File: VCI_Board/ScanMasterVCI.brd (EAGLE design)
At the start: 53 x 39.4 mm, 81 parts, among them IC1 XMEGA16A4A, Q1 MMBT4403, Q10 ZXMP6A17G, Q2 MMBT3904, Q3 MMBT3904, Q4 MMBT3904, Q5 MMBT3904, Q6 MMBT3904, Q7 NTZD5110N, Q8 NTZD5110N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

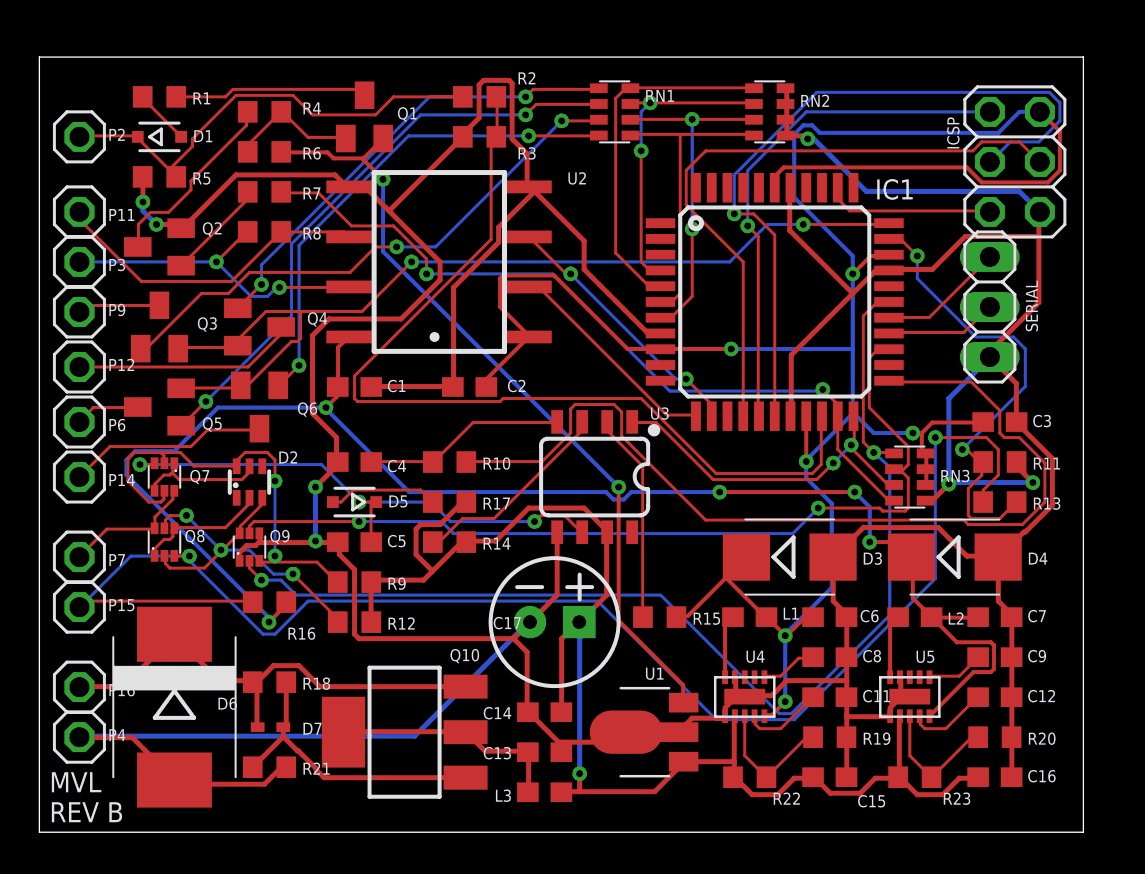
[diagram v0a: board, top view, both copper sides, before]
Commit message: Added Mini USB connector, beefed up traces
Doing more corrections that needed doing, +12V/GND traces are all 12 mil now, +5V/+8V/+3.3V traces are all 10 mil. Kept the rest as 6 mil for now. Rather than use a separate IC to do proper RS-232 communication to a PC, I am instead just going to use a Mini USB connector for PC connection based on what I've seen in the XMEGA data sheet. Changed the ICSP header to be a PDI header, since XMEGA apparently can't be programmed over ICSP.
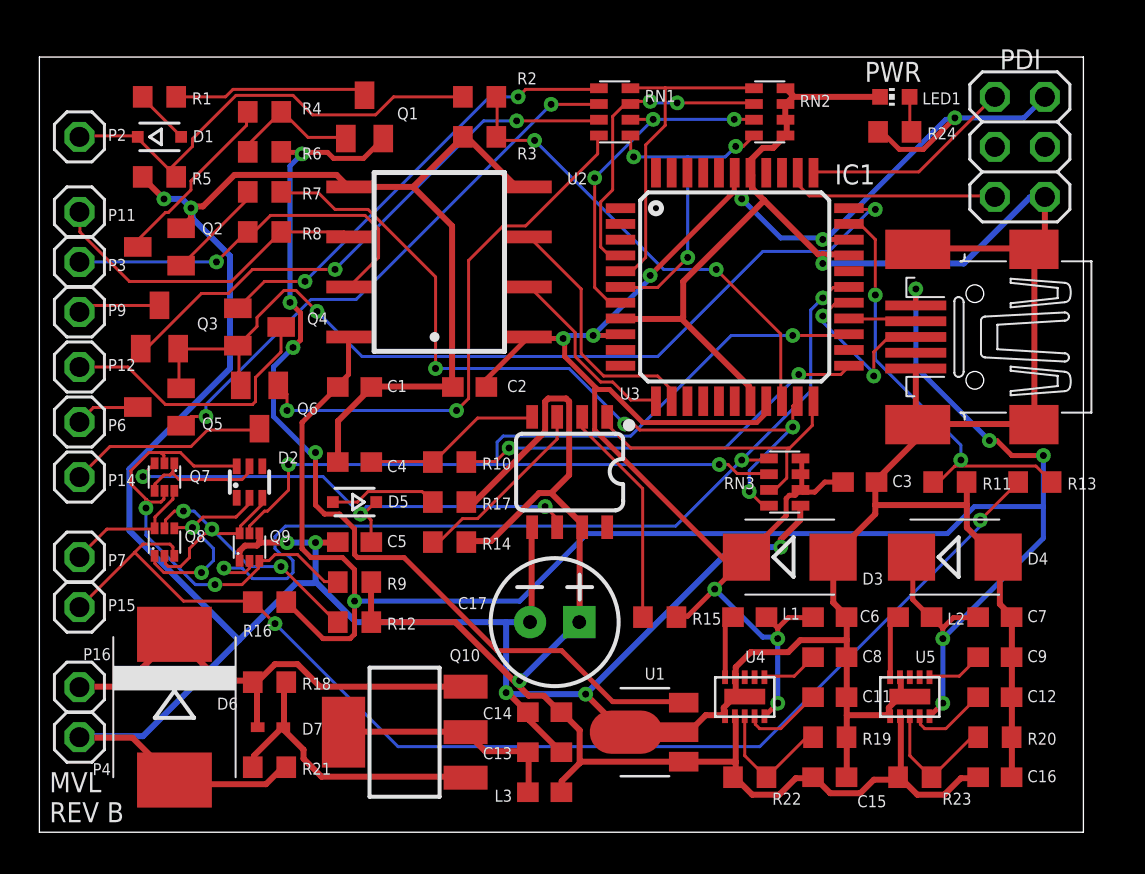
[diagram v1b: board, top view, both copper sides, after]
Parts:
- removed ICSP: (no value), pinhead:2X03
- removed SERIAL: (no value), pinhead:1X03
- added LED1: (no value), led:CHIP-LED0603
- added PDI: (no value), pinhead:2X03
- added R24: 120, resistor:R0603
- added X1: MINI-USB-SCHIELD-32005-201, con-cypressindustries:32005-201
- C13: value 0.1uF -> 0.1uF 25V
- C14: value 330pF -> 330pF 16V
- C17: value 100uF -> 100uF 25V
- D3: value SMLVT3V3 -> SMBJ3V3HE3
- moved C3 7.74 mm to (41.7, 17.8)
- moved RN3 6.36 mm to (37.8, 17.8)
- moved R11 2.74 mm to (46.2, 17.8)
- moved IC1 2.17 mm to (35.3, 27.7)
- moved R13 2.05 mm to (50.5, 17.8)
- moved U3 1.30 mm to (26.9, 18.3)
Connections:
- removed net MISO: IC1.16, ICSP.1
- removed net MOSI: IC1.15, ICSP.4
- removed net PC-RX: IC1.26, SERIAL.2
- removed net PC-TX: IC1.27, SERIAL.1
- removed net RESET: IC1.35, ICSP.5
- removed net SCK: IC1.17, ICSP.3
- new net N$2: LED1.A, R24.1
- new net N$24: IC1.27, X1.3
- new net N$25: IC1.26, X1.4
- new net PDI_CLK: IC1.35, PDI.5
- new net PDI_DATA: IC1.34, PDI.1
- net +3V3: now also PDI.2, R24.2; no longer ICSP.2
- net +5V: now also X1.5
- net GND: now also LED1.C, PDI.6, X1.1, X1.M1, X1.M2, X1.M3, X1.M4; no longer ICSP.6, SERIAL.3
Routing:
- net SCK: track 37.5 -> 0.00 mm, vias 1 -> 0
- net MOSI: track 32.7 -> 0.00 mm
- net MISO: track 26.2 -> 0.00 mm, vias 1 -> 0
- net ISO-K-TX: track 47.3 -> 21.5 mm, vias 0 -> 2
- net +3V3: track 119.8 -> 97.4 mm, vias 6 -> 9
- net J1850VPW-RX: track 46.4 -> 24.1 mm, vias 0 -> 2
- net +5V: track 77.4 -> 95.1 mm, vias 5 -> 6
- net J1962-15: track 75.8 -> 61.3 mm
- net PDI_CLK: track 0.00 -> 10.9 mm
- net PDI_DATA: track 0.00 -> 10.8 mm
- net SCI-A-TX-EN: track 56.4 -> 46.3 mm, vias 2 -> 3
- net N$24: track 0.00 -> 9.41 mm, vias 0 -> 2
- net +8V: track 40.1 -> 49.4 mm, vias 2 -> 4
- net RESET: track 8.57 -> 0.00 mm
- net +12V: track 70.8 -> 77.9 mm
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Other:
- board text added: "PWR"

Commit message: Added extra protection and pull-down resistors to USB circuit, added a pull-up resistor to PDI circuit.
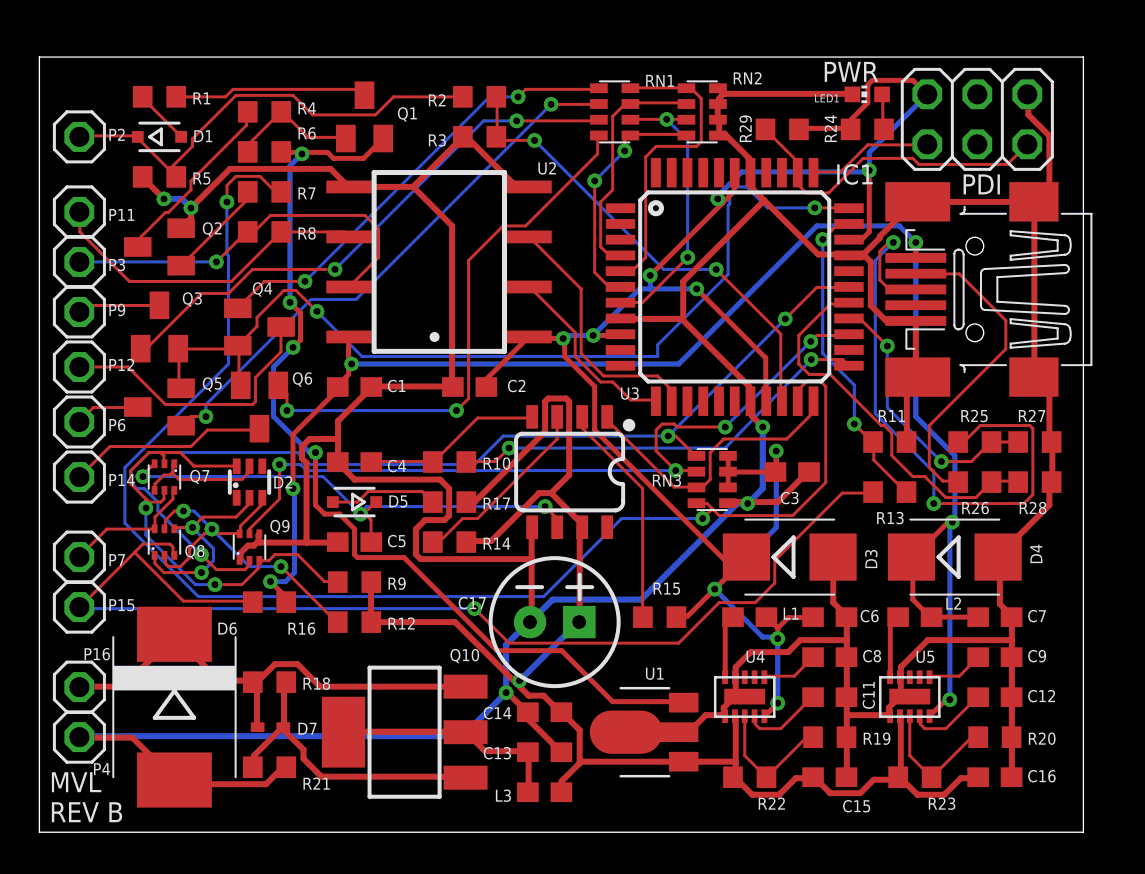
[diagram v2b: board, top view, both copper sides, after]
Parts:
- added R25, R26: 33, adafruit:R0603
- added R27, R28: 15k, adafruit:R0603
- added R29: 1k, adafruit:R0603
- IC1: value XMEGA16A4A -> XMEGA16A4U
- LED1: value (none) -> RED
- moved R13 7.38 mm to (43.2, 17.3)
- moved RN3 3.69 mm to (34.2, 17.9)
- moved R11 3.66 mm to (43.2, 19.8)
- moved C3 3.47 mm to (38.2, 18.3)
- moved RN2 3.43 mm to (33.7, 36.6)
- moved PDI 2.57 mm to (47.6, 36.2), turned to 0 degrees
- moved X1 2.41 mm to (47.5, 27.6)
- moved LED1 1.40 mm to (42.0, 37.5)
- moved R24 1.40 mm to (42.0, 35.7)
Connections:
- new net USB_D+: IC1.26, R25.2, R27.1
- new net USB_D-: IC1.27, R26.2, R28.1
- net +3V3: now also R29.2
- net GND: now also R27.2, R28.2
- net N$24: now also R25.1; no longer IC1.27
- net N$25: now also R26.1; no longer IC1.26
- net PDI_CLK: now also R29.1
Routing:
- net J1850VPW-TX: track 40.7 -> 70.6 mm, vias 4 -> 2
- net N$24: track 9.41 -> 32.0 mm
- net USB_D-: track 0.00 -> 19.7 mm
- net USB_D+: track 0.00 -> 13.8 mm, vias 0 -> 2
- net N$25: track 3.44 -> 16.4 mm
- net +5V: track 95.1 -> 83.0 mm
- net ISO-K-EN: track 50.3 -> 39.9 mm, vias 3 -> 4
- net GND: track 288.2 -> 280.3 mm, vias 8 -> 5
- net PDI_CLK: track 10.9 -> 16.6 mm
- net SCI-A-TX-EN: track 46.3 -> 51.7 mm
- net +3V3: track 97.4 -> 102.3 mm, vias 9 -> 10
- net SCI-RX: track 21.7 -> 16.9 mm
- net SCI-A-TRANS-EN: track 16.9 -> 12.3 mm, vias 3 -> 2
- net PDI_DATA: track 10.8 -> 6.38 mm
- net SCI-A-ENGINE-EN: track 15.7 -> 12.2 mm, vias 2 -> 0
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
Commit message: Changed Mini-USB to Micro, changed XMEGA
Decided to switch to MicroUSB because it's cheaper, smaller, and I have more micro cables laying around. I noticed that I am using the A4 XMEGA, which does not have USB. I am going to then order the A4U XMEGA which has USB, and I am going to consider upgrading to the 32 kB version.
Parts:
- removed X1: MINI-USB-SCHIELD-32005-201, con-cypressindustries:32005-201
- added U$1: MICRO_USB, customics:10118192
- IC1: value XMEGA16A4U -> XMEGA32A4U
- moved R27 11.1 mm to (45.7, 29.8)
- moved R25 8.20 mm to (45.7, 27.8), turned to 180 degrees
- moved R26 8.20 mm to (45.7, 25.8), turned to 180 degrees
- moved R28 7.68 mm to (45.7, 23.7)
- moved C3 7.52 mm to (45.7, 17.7)
- moved R13 3.50 mm to (45.7, 19.7)
- moved R11 3.17 mm to (45.7, 21.7)
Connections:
- net +5V: now also U$1.1; no longer X1.5
- net GND: now also U$1.5, U$1.M1, U$1.M2, U$1.M3, U$1.M4, U$1.M5, U$1.M6; no longer X1.1, X1.M1, X1.M2, X1.M3, X1.M4
- net N$24: now also U$1.3; no longer X1.3
- net N$25: now also U$1.2; no longer X1.4
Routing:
- net N$24: track 32.0 -> 1.98 mm, vias 2 -> 0
- net N$25: track 16.4 -> 1.92 mm
- net USB_D-: track 19.7 -> 6.32 mm
- net +3V3: track 102.3 -> 112.7 mm, vias 10 -> 9
- net GND: track 280.3 -> 285.1 mm
- net +5V: track 83.0 -> 87.1 mm, vias 6 -> 4
- net J1962-15: track 58.6 -> 60.4 mm, vias 1 -> 2
- net SCI-RX: track 16.9 -> 15.8 mm
- net USB_D+: track 13.8 -> 13.6 mm, vias 2 -> 0

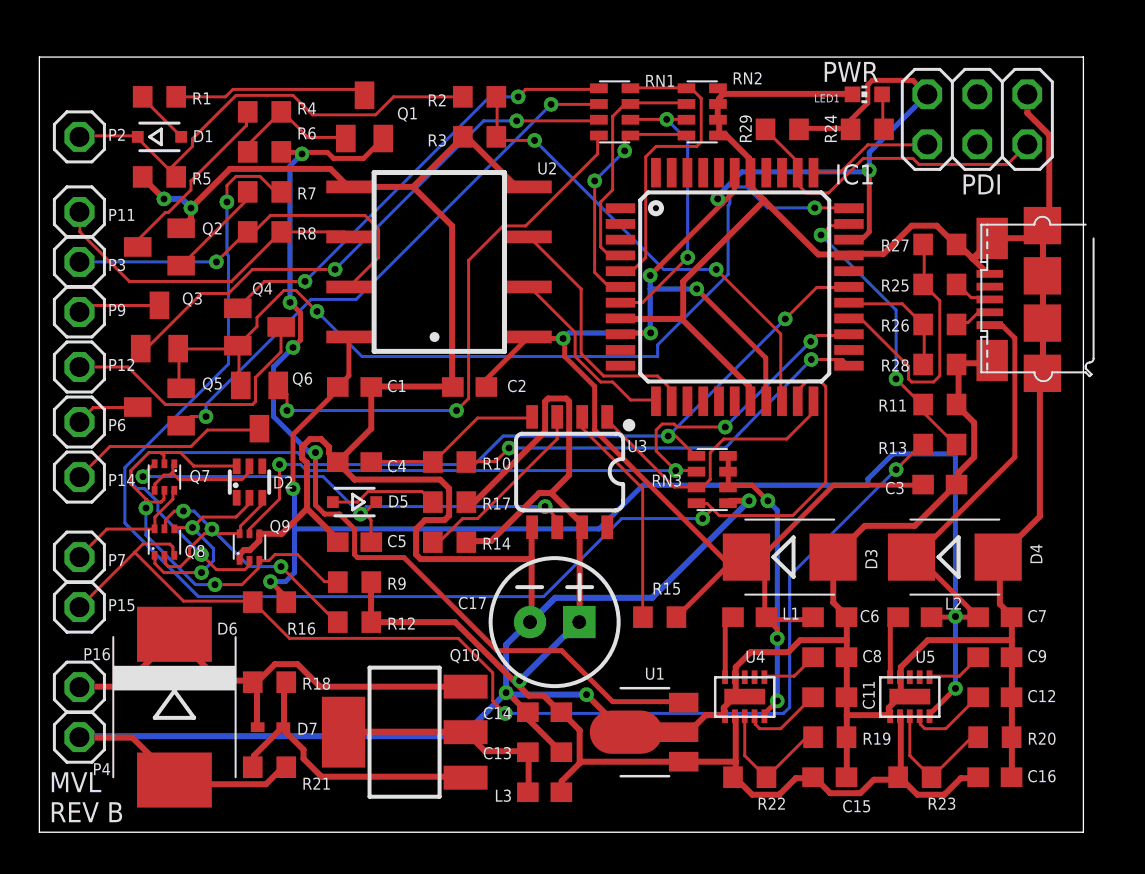
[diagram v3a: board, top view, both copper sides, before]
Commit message: Some final tweaks before sending out. USB data wires from XMEGA were reversed, fixed. Some small nit-picks with power nets, other than that, it is done. Ordering another set of boards.
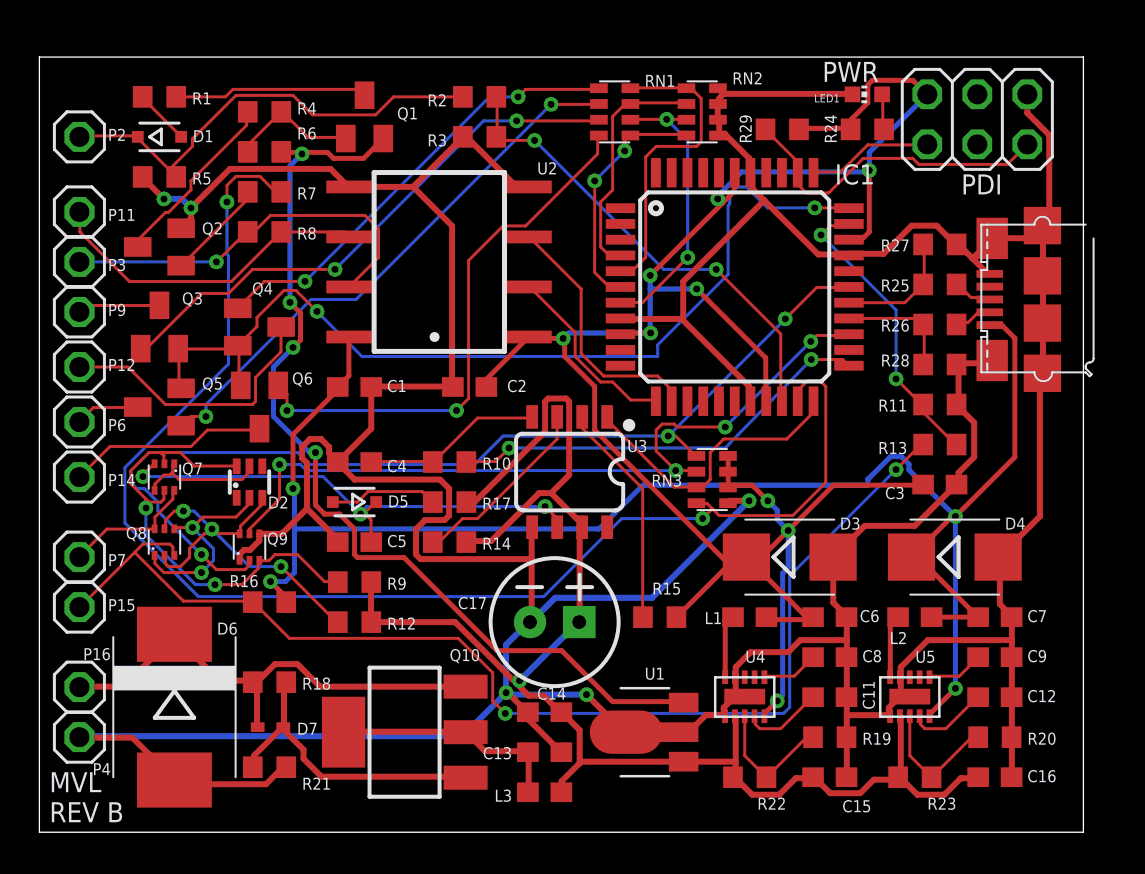
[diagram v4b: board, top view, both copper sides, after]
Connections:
- net USB_D+: now also IC1.27; no longer IC1.26
- net USB_D-: now also IC1.26; no longer IC1.27
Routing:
- net USB_D+: track 13.6 -> 6.25 mm
- net +5V: track 87.1 -> 85.5 mm
- net +3V3: track 112.7 -> 113.5 mm
